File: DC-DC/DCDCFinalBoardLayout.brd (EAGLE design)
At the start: 127.9 x 114.3 mm, 37 parts, among them J1 1200845133, K1 ALZ12B12W

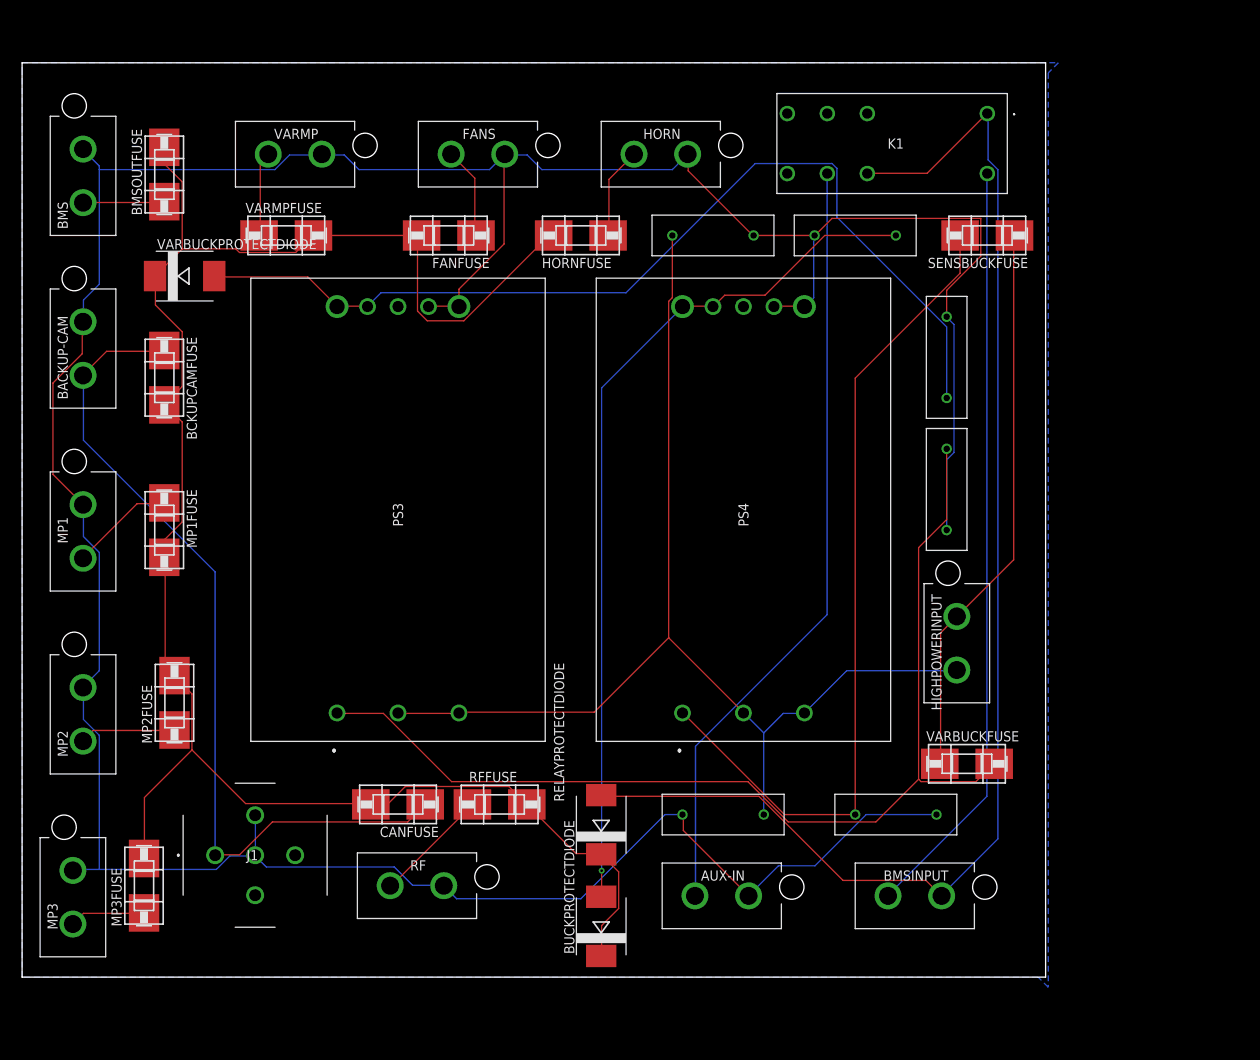
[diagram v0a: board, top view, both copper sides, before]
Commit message: made DCDC traces thicc
slid wires around to fix DRCs

ready to fab
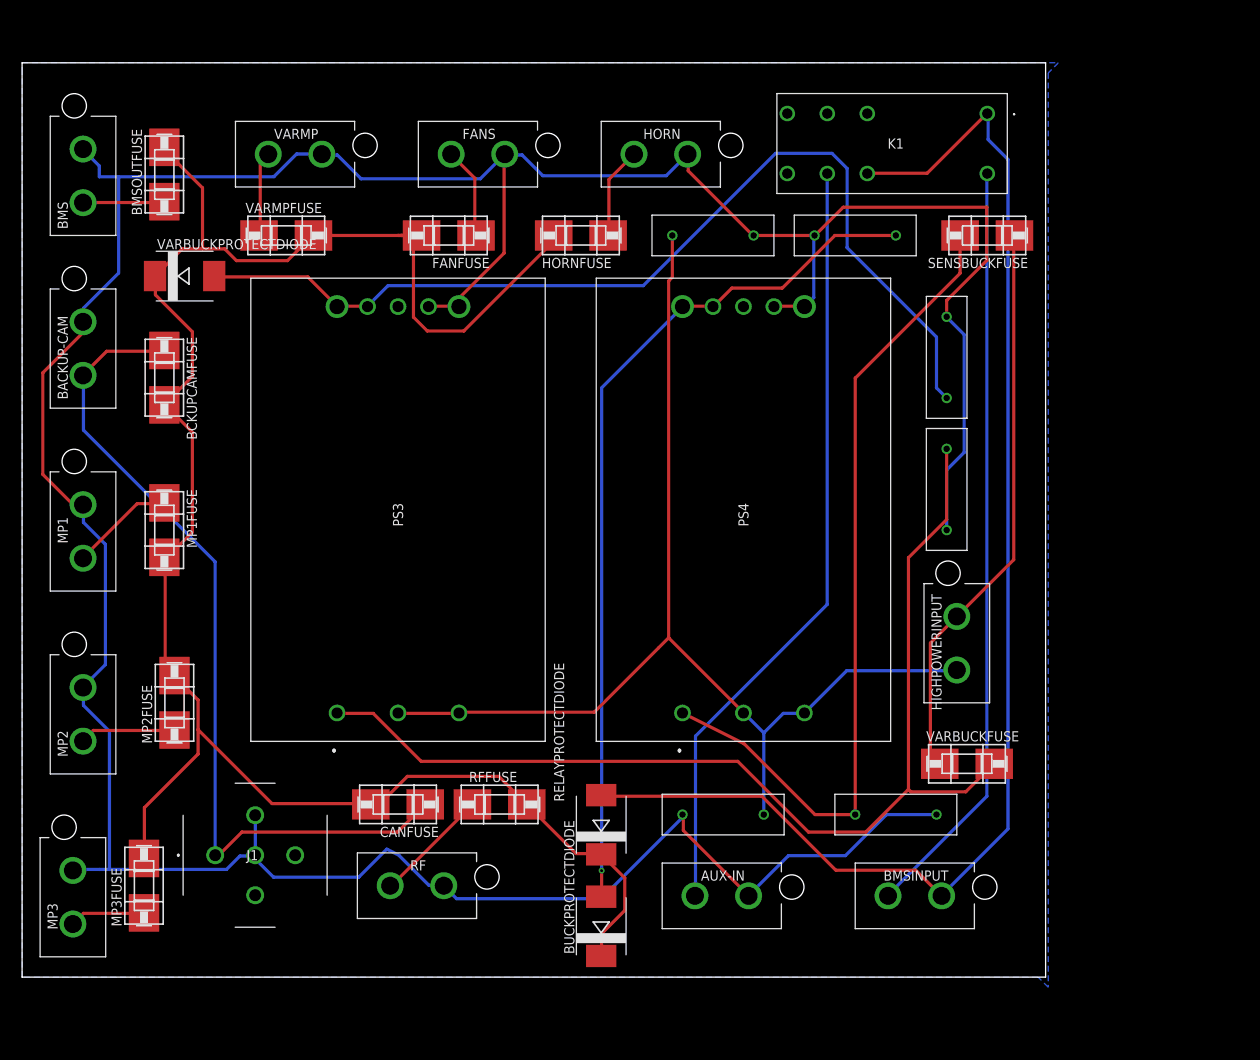
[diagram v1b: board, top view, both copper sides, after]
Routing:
- net GND: track 428.0 -> 441.1 mm
- net 12V: track 234.9 -> 247.5 mm
- net N$5: track 133.8 -> 136.7 mm
- net N$13: track 121.6 -> 123.4 mm
- net N$4: track 167.2 -> 168.3 mm
- net IN+: track 70.0 -> 70.9 mm
- net N$9: track 104.7 -> 104.0 mm

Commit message: DCDC - added top GND plane
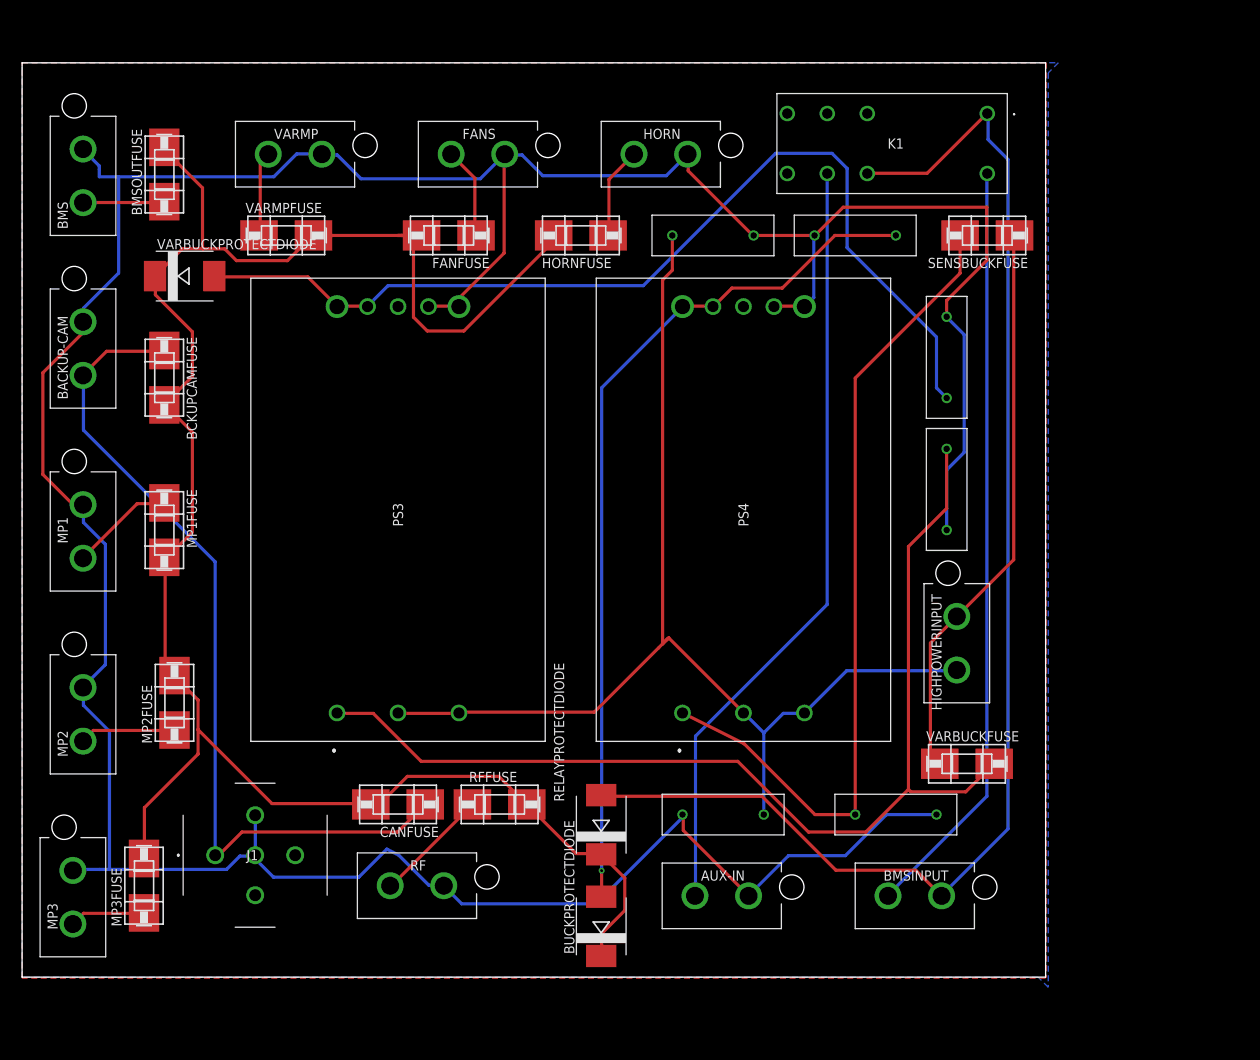
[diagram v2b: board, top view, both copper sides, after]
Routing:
- net IN(-): track 142.8 -> 144.8 mm
- net GND: track 441.1 -> 441.7 mm
- added copper zone on layer 1, net GND
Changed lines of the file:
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@@
 <wire x1="8.9104" y1="133.99" x2="5.1308" y2="137.7696" width="0.4" layer="1"/>
 <wire x1="10.0584" y1="156.8196" x2="10.16" y2="156.85" width="0.4" layer="1"/>
-<wire x1="74.93" y1="84.7344" x2="85.09" y2="94.8944" width="0.4" layer="16"/>
-<wire x1="56.8452" y1="84.7344" x2="74.93" y2="84.7344" width="0.4" layer="16"/>
-<wire x1="55.3212" y1="86.2584" x2="56.8452" y2="84.7344" width="0.4" layer="16"/>
+<wire x1="74.295" y1="84.0994" x2="85.09" y2="94.8944" width="0.4" layer="16"/>
+<wire x1="57.4802" y1="84.0994" x2="74.295" y2="84.0994" width="0.4" layer="16"/>
+<wire x1="55.3212" y1="86.2584" x2="57.4802" y2="84.0994" width="0.4" layer="16"/>
 <wire x1="55.3212" y1="86.2584" x2="55.25" y2="86.36" width="0.4" layer="16"/>
 <wire x1="36.8554" y1="177.8254" x2="39.9846" y2="177.8254" width="0.4" layer="16"/>
@@
 <wire x1="12.192" y1="88.392" x2="13.462" y2="88.392" width="0.4" layer="16"/>
 <wire x1="12.192" y1="174.9806" x2="14.605" y2="174.9806" width="0.4" layer="16"/>
+<polygon width="0.1524" layer="1">
+<vertex x="2.54" y="189.23"/>
+<vertex x="130.556" y="189.23"/>
+<vertex x="130.556" y="74.93"/>
+<vertex x="130.429" y="74.803"/>
+<vertex x="2.54" y="74.803"/>
+</polygon>
 </signal>
 <signal name="12V">
@@
 <wire x1="53.1876" y1="155.702" x2="57.7596" y2="155.702" width="0.4" layer="1"/>
 <wire x1="53.1876" y1="155.702" x2="51.4604" y2="157.4292" width="0.4" layer="1"/>
-<wire x1="51.4604" y1="167.64" x2="51.4604" y2="167.132" width="0.4" layer="1"/>
 <wire x1="27.8638" y1="165.9636" x2="25.0952" y2="165.9636" width="0.4" layer="1"/>
 <wire x1="29.337" y1="164.4904" x2="27.8638" y2="165.9636" width="0.4" layer="1"/>
@@
 <wire x1="20.6792" y1="127.41" x2="20.32" y2="127.41" width="0.4" layer="1"/>
 <wire x1="68.99" y1="166.9324" x2="68.99" y2="167.64" width="0.4" layer="1"/>
-<wire x1="51.4604" y1="167.64" x2="50.927" y2="167.64" width="0.4" layer="1"/>
+<wire x1="51.4604" y1="167.64" x2="51.435" y2="167.64" width="0.4" layer="1"/>
+<wire x1="51.435" y1="167.64" x2="50.927" y2="167.64" width="0.4" layer="1"/>
 <wire x1="50.927" y1="167.64" x2="49.911" y2="167.64" width="0.4" layer="1"/>
 <wire x1="49.911" y1="167.64" x2="49.53" y2="167.64" width="0.4" layer="1"/>
@@
 <wire x1="50.927" y1="167.64" x2="49.911" y2="167.64" width="0.4" layer="1"/>
 <wire x1="51.4604" y1="157.4292" x2="51.4604" y2="157.4292" width="0.4" layer="1"/>
-<wire x1="51.4604" y1="157.4292" x2="51.4604" y2="167.64" width="0.4" layer="1"/>
-<wire x1="49.53" y1="167.64" x2="52.48" y2="167.64" width="0.4" layer="1"/>
+<wire x1="49.53" y1="167.64" x2="51.435" y2="167.64" width="0.4" layer="1"/>
+<wire x1="51.435" y1="167.64" x2="52.48" y2="167.64" width="0.4" layer="1"/>
+<wire x1="51.4604" y1="157.4292" x2="51.4604" y2="167.6146" width="0.4" layer="1"/>
+<wire x1="51.4604" y1="167.6146" x2="51.435" y2="167.64" width="0.4" layer="1"/>
 </signal>
 <signal name="IN+">
@@
 <wire x1="49.53" y1="107.8992" x2="49.53" y2="107.95" width="0.4" layer="1"/>
 <wire x1="57.15" y1="107.8992" x2="57.15" y2="107.95" width="0.4" layer="1"/>
-<wire x1="83.82" y1="162.4076" x2="83.82" y2="167.64" width="0.4" layer="1"/>
-<wire x1="83.3628" y1="161.9504" x2="83.82" y2="162.4076" width="0.4" layer="1"/>
-<wire x1="83.3628" y1="117.348" x2="83.3628" y2="161.9504" width="0.4" layer="1"/>
+<wire x1="83.82" y1="163.2966" x2="83.82" y2="167.64" width="0.4" layer="1"/>
+<wire x1="82.6008" y1="162.0774" x2="83.82" y2="163.2966" width="0.4" layer="1"/>
+<wire x1="82.6008" y1="116.586" x2="82.6008" y2="162.0774" width="0.4" layer="1"/>
 <wire x1="92.6592" y1="108.0516" x2="83.3628" y2="117.348" width="0.4" layer="1"/>
 <wire x1="92.6592" y1="108.0516" x2="92.71" y2="107.95" width="0.4" layer="1"/>
@@
 <wire x1="100.2792" y1="107.8992" x2="100.33" y2="107.95" width="0.4" layer="16"/>
 <wire x1="74.0664" y1="108.0516" x2="57.15" y2="108.0516" width="0.4" layer="1"/>
-<wire x1="83.3628" y1="117.348" x2="82.0928" y2="116.078" width="0.4" layer="1"/>
+<wire x1="83.3628" y1="117.348" x2="83.2358" y2="117.221" width="0.4" layer="1"/>
 <wire x1="57.15" y1="108.0516" x2="57.15" y2="107.95" width="0.4" layer="1"/>
 <wire x1="105.6132" y1="113.2332" x2="119.3292" y2="113.2332" width="0.4" layer="16"/>
@@
 <wire x1="119.3292" y1="113.2332" x2="119.38" y2="113.32" width="0.4" layer="16"/>
 <wire x1="82.0928" y1="116.078" x2="74.0664" y2="108.0516" width="0.4" layer="1"/>
+<wire x1="83.1088" y1="117.094" x2="82.0928" y2="116.078" width="0.4" layer="1"/>
+<wire x1="83.2358" y1="117.221" x2="83.1088" y2="117.094" width="0.4" layer="1"/>
+<wire x1="83.2358" y1="117.221" x2="82.6008" y2="116.586" width="0.4" layer="1"/>
 </signal>
 <signal name="N$1">
@@
 <contactref element="VARBUCKFUSE" pad="P$2"/>
 <contactref element="PS3" pad="1"/>
-<wire x1="118.11" y1="132.1308" x2="118.11" y2="140.97" width="0.4" layer="1"/>
-<wire x1="113.3348" y1="127.3556" x2="118.11" y2="132.1308" width="0.4" layer="1"/>
-<wire x1="113.3348" y1="98.3996" x2="113.3348" y2="127.3556" width="0.4" layer="1"/>
+<wire x1="118.11" y1="133.5278" x2="118.11" y2="140.97" width="0.4" layer="1"/>
+<wire x1="113.3348" y1="128.7526" x2="118.11" y2="133.5278" width="0.4" layer="1"/>
+<wire x1="113.3348" y1="98.3996" x2="113.3348" y2="128.7526" width="0.4" layer="1"/>
 <wire x1="113.6396" y1="98.0948" x2="113.3348" y2="98.3996" width="0.4" layer="1"/>
 <wire x1="120.4976" y1="98.0948" x2="113.6396" y2="98.0948" width="0.4" layer="1"/>

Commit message: DCDC added CAN
generated gerbers for a lot of stuff
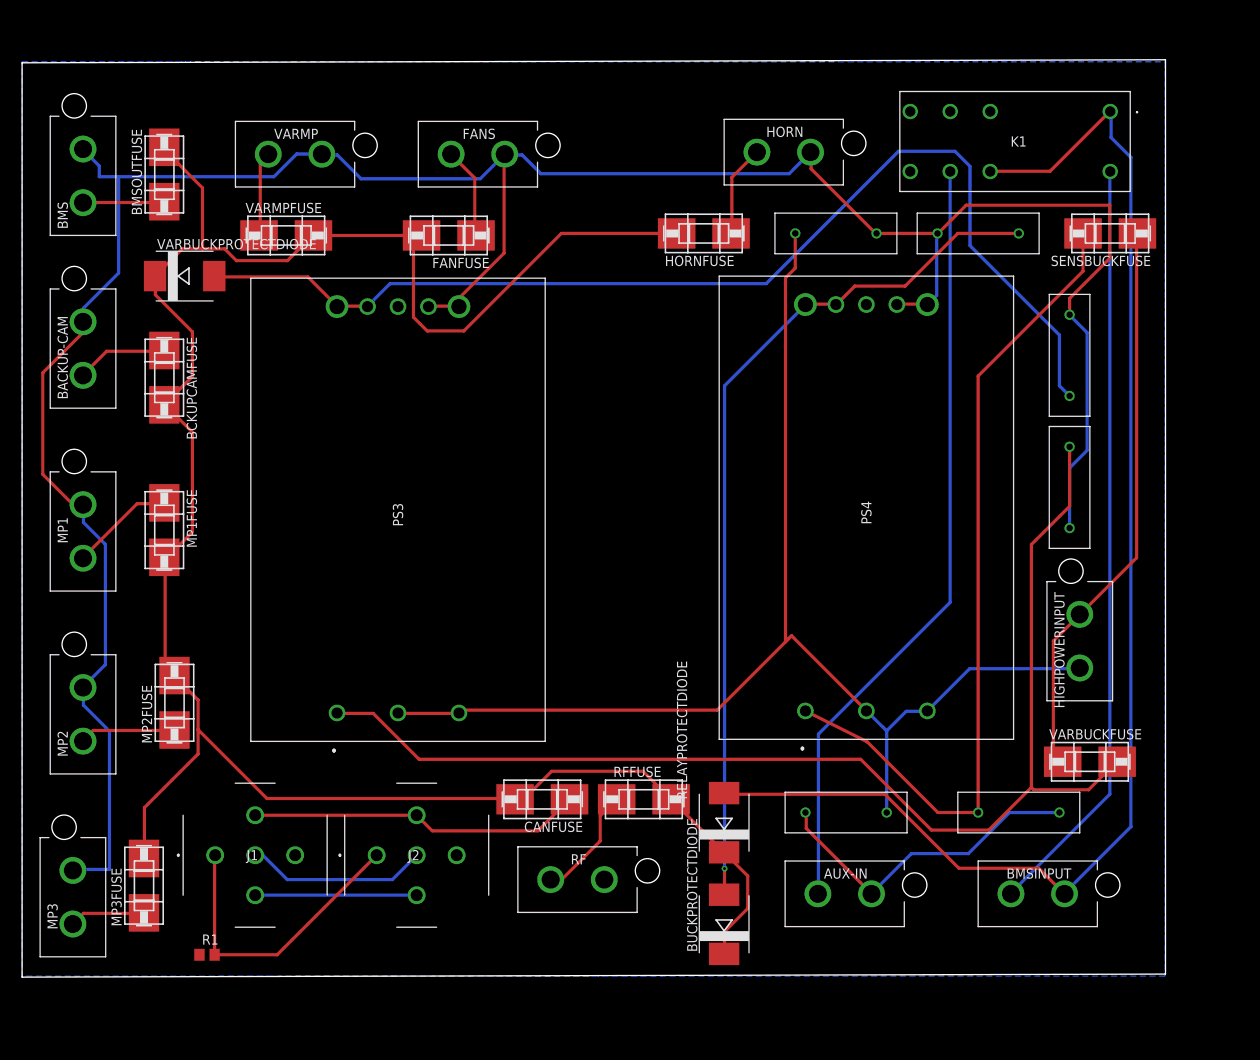
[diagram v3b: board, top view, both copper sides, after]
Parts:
- added J2: 1200845133, SamacSys_Parts:1200845133
- added R1: 0, eagle-ltspice:R0805
- moved RF 20.1 mm to (64.5, 87.1)
- moved RFFUSE 18.0 mm to (80.3, 97.2)
- moved CANFUSE 18.0 mm to (67.6, 97.2)
- moved HIGHPOWERINPUT 15.4 mm to (134.7, 109.5)
- moved AUX-IN 15.4 mm to (97.9, 85.3)
- moved HORNFUSE 15.4 mm to (87.8, 167.9)
- moved U$1 15.4 mm to (110.6, 95.5)
- moved U$3 15.4 mm to (99.2, 167.9)
- moved U$5 15.4 mm to (117.0, 167.9)
- moved U$7 15.4 mm to (133.5, 131.1)
- moved U$8 15.4 mm to (133.5, 157.7)
- moved BMSINPUT 15.4 mm to (122.0, 85.3)
- moved BUCKPROTECTDIODE 15.4 mm to (90.3, 81.5)
- moved HORN 15.4 mm to (90.3, 178.1)
- moved K1 15.4 mm to (138.6, 183.1)
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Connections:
- removed net CAN_H: J1.3
- removed net CAN_L: J1.4
- new net N$16: CANFUSE.P$1, J1.2, J2.2
- new net N$17: J1.1, J2.1, R1.2
- new net N$18: J1.4, J2.4
- new net N$20: J1.MH1, J2.MH1
- net CAN+: no longer CANFUSE.P$1, J1.1
- net GND: now also J1.3, J2.3, R1.1; no longer J1.2, J1.MH1
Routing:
- net CAN+: track 107.2 -> 11.5 mm
- net GND: track 441.7 -> 369.6 mm
- net N$16: track 0.00 -> 41.7 mm
- net N$17: track 0.00 -> 37.9 mm
- net 12V: track 247.0 -> 274.4 mm
- net N$20: track 0.00 -> 22.7 mm
- net N$18: track 0.00 -> 20.2 mm
- net N$13: track 123.4 -> 138.8 mm
- net IN(-): track 144.8 -> 160.2 mm
- net N$5: track 136.7 -> 151.9 mm
- removed copper zone on layer 1, net GND
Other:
- board size 127.9 x 114.3 mm -> 142.9 x 114.7 mm

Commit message: DCDC Final Board Layout & Schematic
The final iteration of a lengthy design process, involving input from a variety of parties, with specializations ranging from physics, to electrical engineering, to electrical engineering, to electrical engineering. Peace and Love :100:
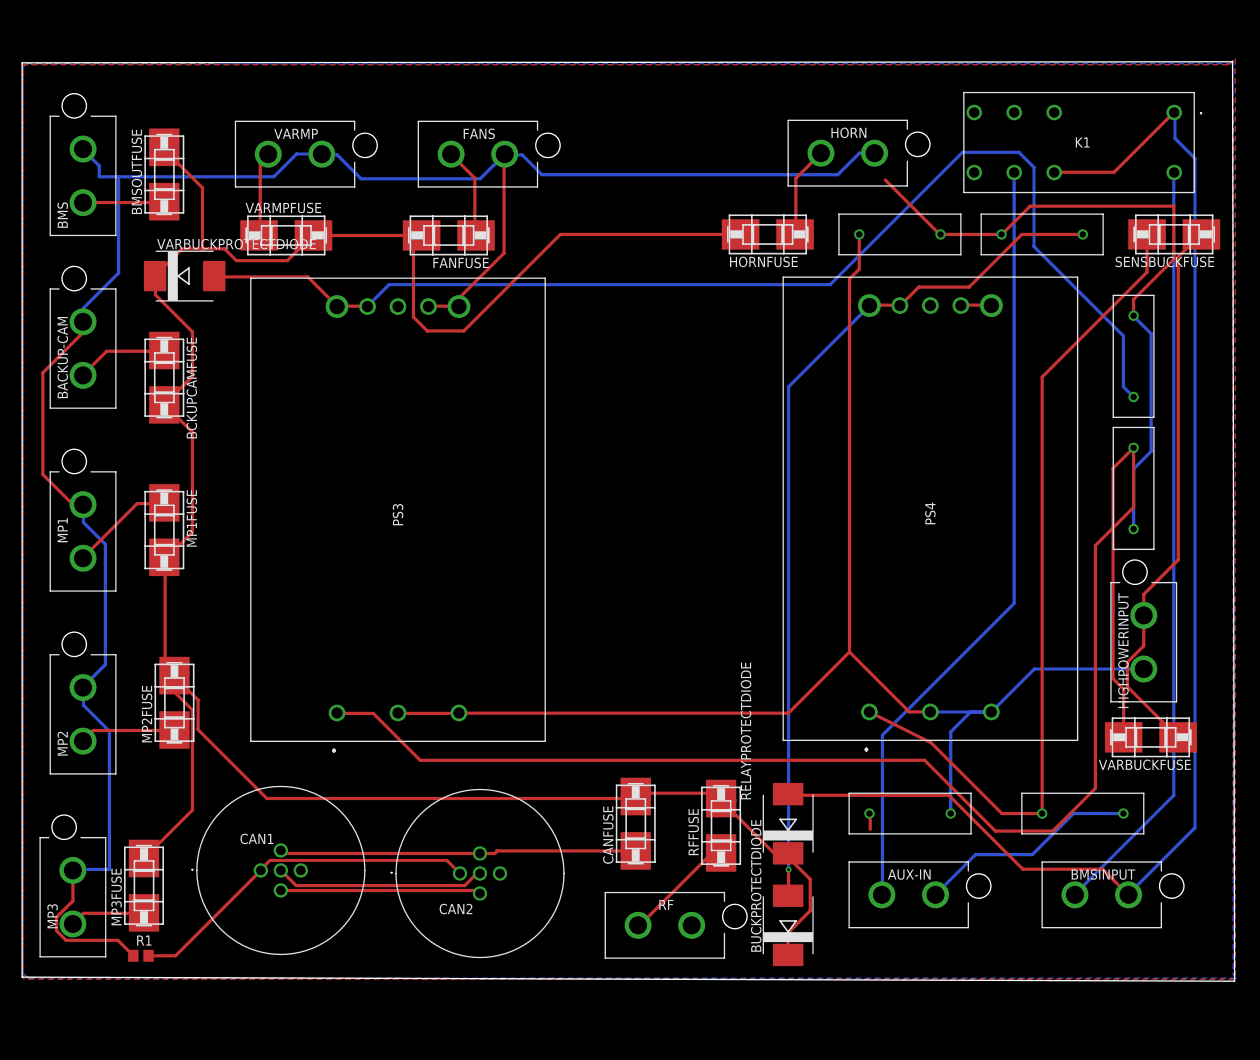
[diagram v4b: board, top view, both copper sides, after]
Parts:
- removed J1, J2: 1200845133, SamacSys_Parts:1200845133
- added CAN1, CAN2: 1200845179, SamacSys_Parts:1200845179
- moved RF 12.3 mm to (75.4, 81.4)
- moved CANFUSE 12.1 mm to (79.2, 94.1), turned to 90 degrees
- moved RFFUSE 10.2 mm to (89.9, 93.9), turned to 90 degrees
- moved R1 8.26 mm to (17.4, 77.6)
- moved VARBUCKFUSE 8.21 mm to (143.6, 104.9), turned to 180 degrees
- moved AUX-IN 8.00 mm to (105.9, 85.2)
- moved BMSINPUT 8.00 mm to (130.0, 85.2)
- moved BUCKPROTECTDIODE 8.00 mm to (98.3, 81.4)
- moved HORN 8.00 mm to (98.3, 177.9)
- moved K1 8.00 mm to (146.6, 183.0)
- moved PS4 8.00 mm to (108.5, 108.1)
- moved RELAYPROTECTDIODE 8.00 mm to (98.3, 94.1)
- moved SENSBUCKFUSE 8.00 mm to (146.6, 167.8)
- moved U$3 8.00 mm to (107.2, 167.8)
- moved U$4 8.00 mm to (140.2, 95.4)
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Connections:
- removed net N$16: CANFUSE.P$1, J1.2, J2.2
- new net N$19: CAN1.5, CAN2.5
- net GND: now also CAN1.3, CAN2.3; no longer J1.3, J2.3
- net N$17: now also CAN1.1, CAN2.1; no longer J1.1, J2.1
- net N$18: now also CAN1.4, CAN2.4; no longer J1.4, J2.4
- net N$20: now also CAN1.2, CAN2.2, CANFUSE.P$1; no longer J1.MH1, J2.MH1
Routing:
- net N$16: track 41.7 -> 0.00 mm
- net N$5: track 151.9 -> 185.5 mm
- net 12V: track 274.4 -> 302.3 mm
- net N$19: track 0.00 -> 26.3 mm
- net N$20: track 22.7 -> 44.7 mm
- net IN(-): track 160.2 -> 170.8 mm
- net N$13: track 138.8 -> 146.8 mm
- net N$17: track 37.9 -> 44.6 mm
- net N$18: track 20.2 -> 25.0 mm
- net GND: track 369.6 -> 371.9 mm
- net IN+: track 70.9 -> 69.4 mm
- added copper zone on layer 1, net GND
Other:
- board size 142.9 x 114.7 mm -> 151.6 x 114.9 mm
